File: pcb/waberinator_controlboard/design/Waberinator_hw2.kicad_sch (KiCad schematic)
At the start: 88 parts, among them J1 Conn_01x04_Pin, J17 GX16-4, J18 GX12-4, J19 GX12-4, J2 preconf. cable, J20 GX12-4, J21 GX12-4, J22 GX12-4, J23 GX12-4, J24 GX12-4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

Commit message: [HW] add esp32
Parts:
- removed J4: Conn_01x08_Pin, Connector_PinHeader_2.54mm:PinHeader_1x08_P2.54mm_Vertical, symbol Connector:Conn_01x08_Pin
- added C33, C35: 100nF, Capacitor_SMD:C_0603_1608Metric_Pad1.08x0.95mm_HandSolder, symbol Device:C
- added C34: 100µF, Capacitor_SMD:C_1210_3225Metric_Pad1.33x2.70mm_HandSolder, symbol Device:C
- added C36, C37, C38: 56µF, Capacitor_SMD:C_Elec_5x5.8, symbol Device:C_Polarized
- added FB7: FerriteBead, Capacitor_SMD:C_1210_3225Metric_Pad1.33x2.70mm_HandSolder, symbol Device:FerriteBead
- added J4: Conn_01x06, Connector_PinHeader_2.54mm:PinHeader_1x06_P2.54mm_Vertical, symbol Connector_Generic:Conn_01x06
- added J7: Conn_01x10_Pin, Connector_PinHeader_2.54mm:PinHeader_1x10_P2.54mm_Vertical, symbol Connector:Conn_01x10_Pin
- added Q10, Q8: Q_NPN_BEC, Package_TO_SOT_SMD:SOT-23_Handsoldering, symbol Device:Q_NPN_BEC
- added R1, R2: 100, Resistor_SMD:R_0603_1608Metric_Pad0.98x0.95mm_HandSolder, symbol Device:R
- added R14, R18: 12k, Resistor_SMD:R_0603_1608Metric_Pad0.98x0.95mm_HandSolder, symbol Device:R
- added TP1, TP2, TP3: TestPoint, TestPoint:TestPoint_Pad_1.0x1.0mm, symbol Connector:TestPoint
- added U8: ESP32-WROOM-32, RF_Module:ESP32-WROOM-32, symbol RF_Module:ESP32-WROOM-32
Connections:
- net +3V3: now also C35.1, FB7.1, J7.1 (Pin_1)
- net RET: now also C33.2, C34.2, C35.2, C36.2, C37.2, C38.2, J4.6 (Pin_6), J7.3 (Pin_3), U8.1 (GND), U8.15 (GND), U8.38 (GND), U8.39 (GND)
- net VLed: now also C36.1, C37.1, C38.1
- net ledstring3_drv_en: now also U1.3 (PC14); no longer U1.5 (PF0)
- net ledstring4_drv_en: now also U1.4 (PC15); no longer U1.6 (PF1)
- net swd_swo: now also J7.6 (Pin_6)
- net swd_tck: now also J7.2 (Pin_2)
- net swd_tms: now also J7.4 (Pin_4)
- net usart1_rx_mcu: now also U1.59 (PB7), R1.2; no longer U1.17 (PA3)
- net usart1_tx_mcu: now also U1.58 (PB6), R2.2; no longer U1.16 (PA2)
- net ~{rst}: now also J7.5 (Pin_5)
- net esp32_en: now reaches U1.28 (PB2)
- net esp32_en: now also Q10.3 (C), U8.3 (EN)
- net spare_3: now reaches U1.30 (PB11)
- net spare_3: now also TP1.1
- net spare_4: now reaches U1.33 (PB12)
- net spare_4: now also TP2.1
- net spare_5: now reaches U1.34 (PB13)
- net spare_5: now also TP3.1
- net spare_1: now reaches U1.47 (PF6)
- net spare_1: now also J7.9 (Pin_9)
- net spare_2: now reaches U1.48 (PF7)
- net spare_2: now also J7.10 (Pin_10)
- new net: Q10.1 (B), R14.2
- new net: Q8.1 (B), R18.2
- new net U0RXD_ESP32: J4.3 (Pin_3), U8.34 (RXD0/IO3)
- new net U0TXD_ESP32: J4.2 (Pin_2), U8.35 (TXD0/IO1)
- new net U1RXD_ESP32: R2.1, U8.30 (IO18)
- new net U1TXD_ESP32: R1.1, U8.28 (IO17)
- new net esp32_io0: Q8.3 (C), U8.25 (IO0)
- new net esp32_prog_dtr: J4.1 (Pin_1), Q8.2 (E), R14.1
- new net esp32_prog_rts: J4.5 (Pin_5), Q10.2 (E), R18.1
- new net esp32_vdd: C33.1, C34.1, FB7.2, U8.2 (VDD)
- new net usart2_rx_mcu: J7.7 (Pin_7), U1.17 (PA3)
- new net usart2_tx_mcu: J7.8 (Pin_8), U1.16 (PA2)
- new net vdd_prog: J4.4 (Pin_4)
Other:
- moved on the sheet: J17, J18, J19, J20, J21, J22, J23, J24, J25, J26

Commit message: [HW] finish layout
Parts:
- removed TP3: TestPoint, TestPoint:TestPoint_Pad_1.0x1.0mm, symbol Connector:TestPoint
- added R24: 100, Resistor_SMD:R_0603_1608Metric_Pad0.98x0.95mm_HandSolder, symbol Device:R
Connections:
- net esp32_io0: now also R24.2
- net spare_5: no longer names the net of U1.34 (PB13)
- net spare_5: now also R24.1
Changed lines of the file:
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@@
 	(wire
 		(pts
-			(xy 95.25 236.22) (xy 107.95 236.22)
+			(xy 95.25 236.22) (xy 119.38 236.22)
 		)
 		(stroke
@@
 	(wire
 		(pts
+			(xy 127 236.22) (xy 137.16 236.22)
+		)
+		(stroke
+			(width 0)
+			(type default)
+		)
+	)
+	(wire
+		(pts
 			(xy 335.915 97.155) (xy 356.87 97.155)
 		)
@@
 		)
 	)
+	(label "esp32_io0"
+		(at 127 236.22 0)
+		(fields_autoplaced yes)
+		(effects
+			(font
+				(size 1.27 1.27)
+			)
+			(justify left bottom)
+		)
+	)
 	(label "tim1_ch2_indicator_led2"
 		(at 153.035 247.015 0)
@@
 		)
 	)
-	(label "spare_5"
-		(at 97.79 236.22 0)
-		(fields_autoplaced yes)
-		(effects
-			(font
-				(size 1.27 1.27)
-			)
-			(justify left bottom)
-		)
-	)
 	(label "adc_depth"
 		(at 97.79 162.56 0)
@@
 	)
 	(symbol
-		(lib_id "Connector:TestPoint")
-		(at 107.95 236.22 270)
-		(unit 1)
-		(exclude_from_sim no)
-		(in_bom yes)
-		(on_board yes)
-		(dnp no)
-		(fields_autoplaced yes)
-		(property "Reference" "TP3"
-			(at 113.03 236.22 90)
-			(effects
-				(font
-					(size 1.27 1.27)
-				)
-				(justify left)
-			)
-		)
-		(property "Value" "TestPoint"
-			(at 113.03 237.49 90)
-			(effects
-				(font
-					(size 1.27 1.27)
-				)
-				(justify left)
-				(hide yes)
-			)
-		)
-		(property "Footprint" "TestPoint:TestPoint_Pad_1.0x1.0mm"
-			(at 107.95 241.3 0)
-			(effects
-				(font
-					(size 1.27 1.27)
-				)
-				(hide yes)
-			)
-		)
-		(property "Datasheet" "~"
-			(at 107.95 241.3 0)
-			(effects
-				(font
-					(size 1.27 1.27)
-				)
-				(hide yes)
-			)
-		)
-		(property "Description" ""
-			(at 107.95 236.22 0)
-			(effects
-				(font
-					(size 1.27 1.27)
-				)
-				(hide yes)
-			)
-		)
-		(pin "1"
-		)
-		(instances
-			(project "Waberinator_hw2"
-				(path "/2abe1fd5-5254-4661-ace0-8064915e9450"
-					(reference "TP3")
-					(unit 1)
-				)
-			)
-		)
-	)
-	(symbol
 		(lib_id "Device:C_Polarized")
 		(at 173.355 29.21 0)
@@
 					(unit 1)
 				)
+			)
+		)
+	)
+	(symbol
+		(lib_id "Device:R")
+		(at 123.19 236.22 90)
+		(unit 1)
+		(exclude_from_sim no)
+		(in_bom yes)
+		(on_board yes)
+		(dnp no)
+		(property "Reference" "R24"
+			(at 123.19 236.22 90)
+			(effects
+				(font
+					(size 1.27 1.27)
+				)
+			)
+		)
+		(property "Value" "100"
+			(at 123.19 233.68 90)
+			(effects
+				(font
+					(size 1.27 1.27)
+				)
+			)
+		)
+		(property "Footprint" "Resistor_SMD:R_0603_1608Metric_Pad0.98x0.95mm_HandSolder"
+			(at 123.19 237.998 90)
+			(effects
+				(font
+					(size 1.27 1.27)
+				)
+				(hide yes)
+			)
+		)
+		(property "Datasheet" "~"
+			(at 123.19 236.22 0)
+			(effects
+				(font
+					(size 1.27 1.27)
+				)
+				(hide yes)
+			)
+		)
+		(property "Description" ""
+			(at 123.19 236.22 0)
+			(effects
+				(font
+					(size 1.27 1.27)
+				)
+				(hide yes)
+			)
+		)
+		(pin "2"
+		)
+		(pin "1"
+		)
+		(instances
+			(project "Waberinator_hw2"
+				(path "/2abe1fd5-5254-4661-ace0-8064915e9450"
+					(reference "R24")
+					(unit 1)
+				)

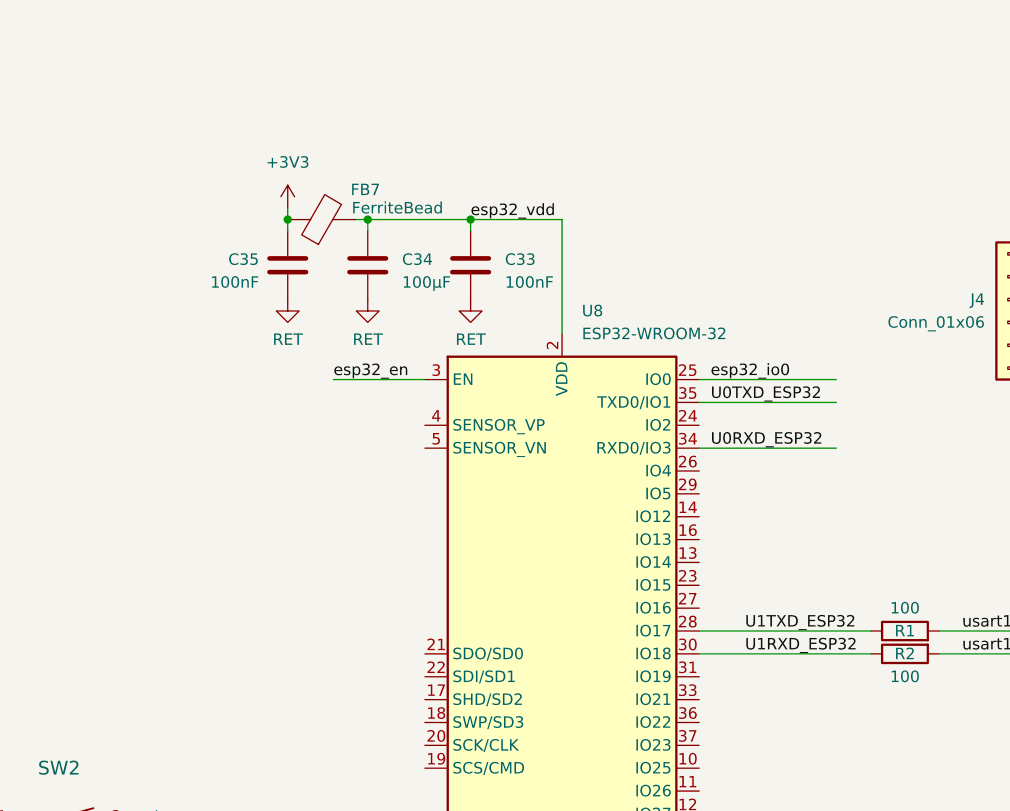
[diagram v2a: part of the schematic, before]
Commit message: [HW/FW] control power state of modem
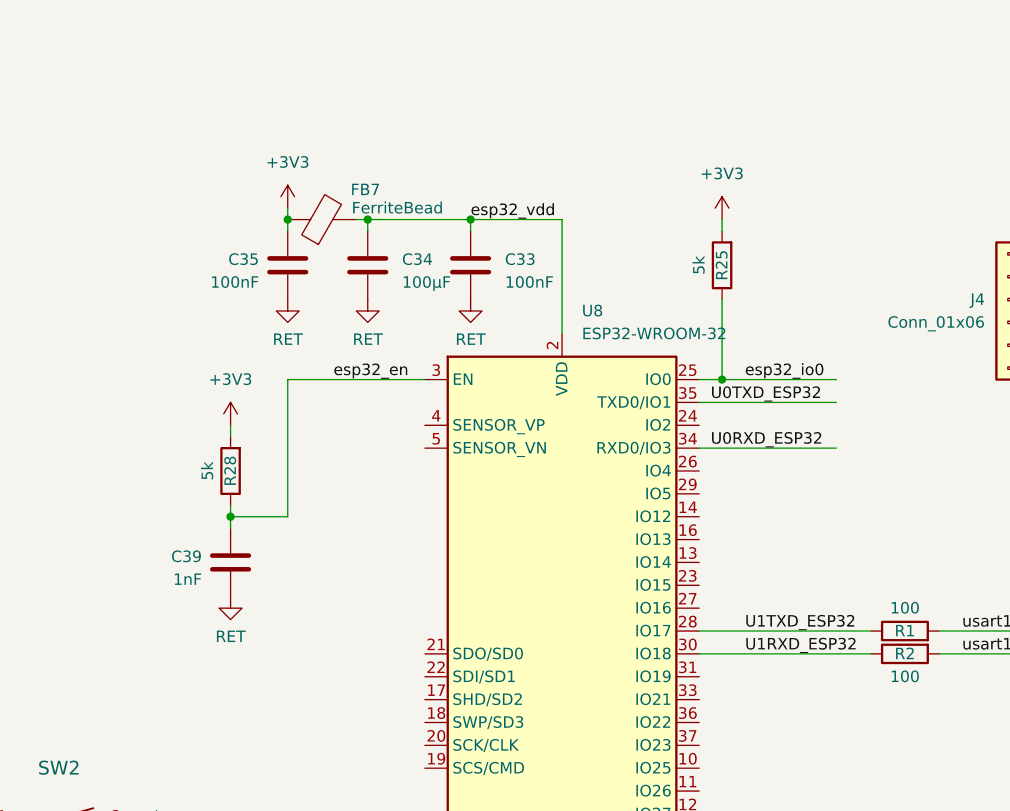
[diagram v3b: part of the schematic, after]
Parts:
- added C39: 1nF, Capacitor_SMD:C_0603_1608Metric_Pad1.08x0.95mm_HandSolder, symbol Device:C
- added R25, R28: 5k, Resistor_SMD:R_0603_1608Metric_Pad0.98x0.95mm_HandSolder, symbol Device:R
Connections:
- net +3V3: now also R25.2, R28.2
- net RET: now also C39.2
- net esp32_en: now also C39.1, R28.1
- net esp32_io0: now also R25.1

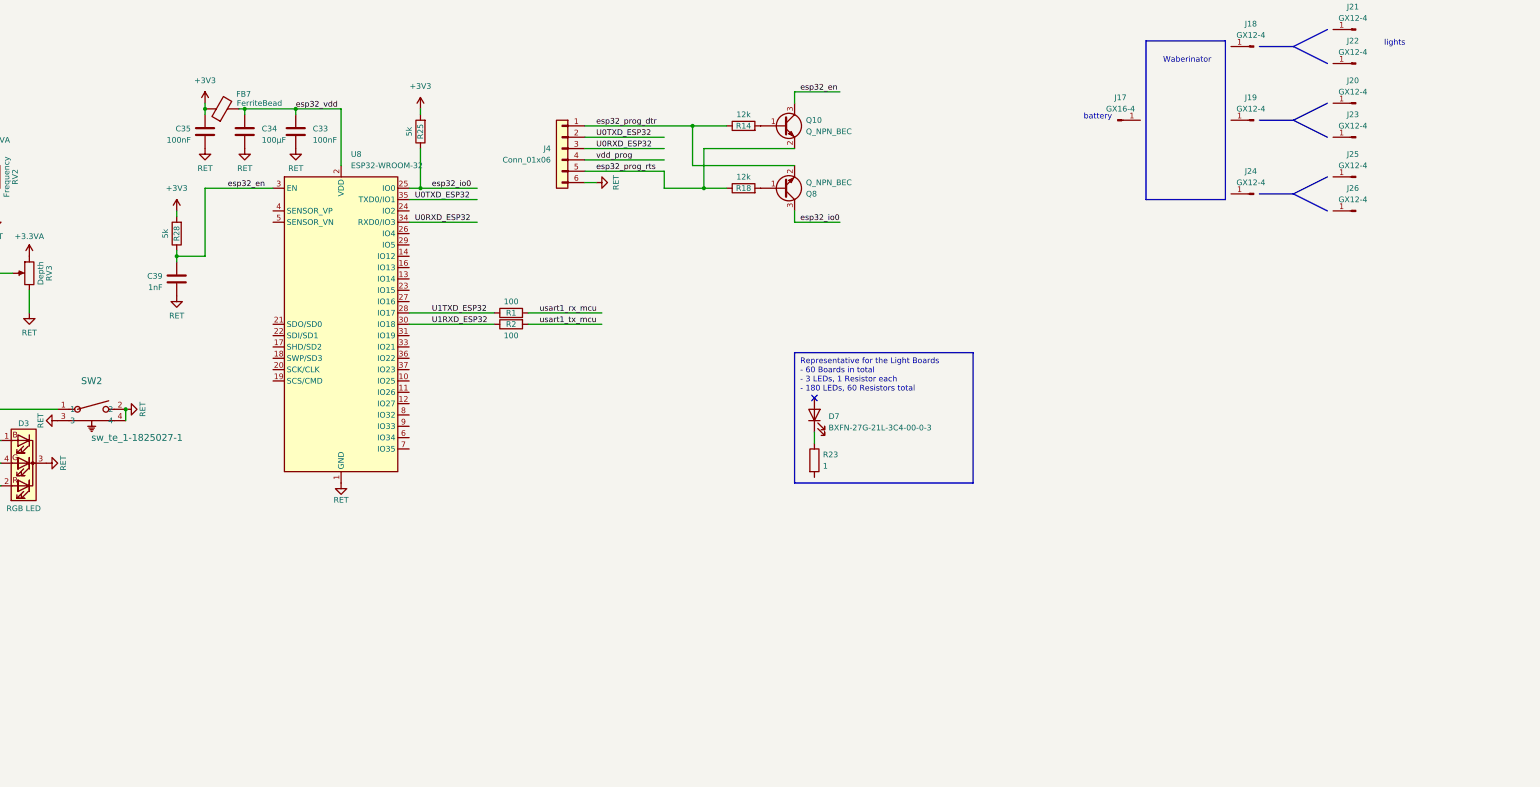
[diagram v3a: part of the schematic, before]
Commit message: [HW] fix esp32 footprint and symbol
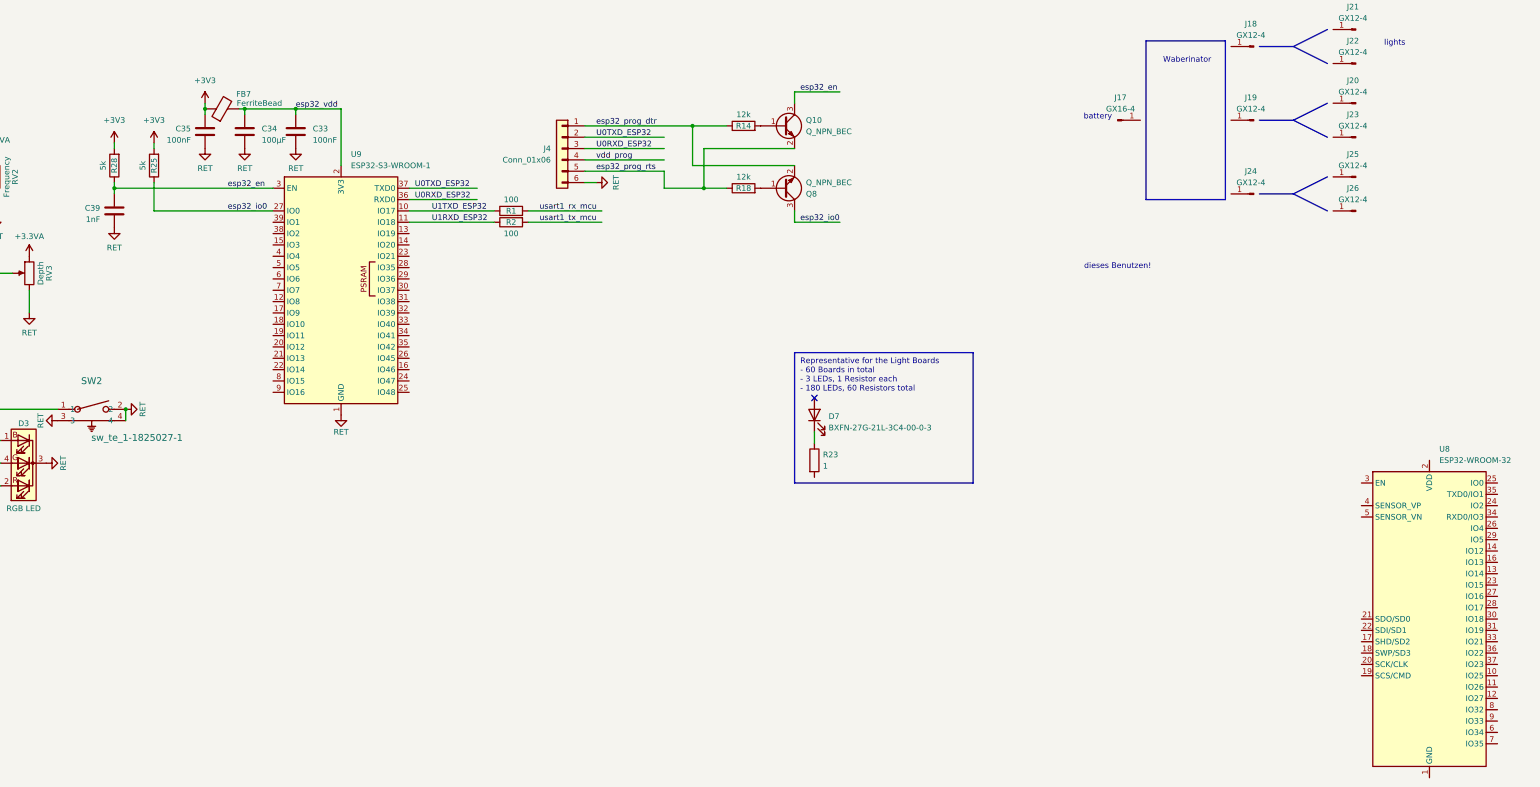
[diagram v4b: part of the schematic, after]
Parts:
- added U9: ESP32-S3-WROOM-1, RF_Module:ESP32-S3-WROOM-1, symbol RF_Module:ESP32-S3-WROOM-1
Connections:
- net RET: now also U9.1 (GND), U9.40 (GND), U9.41 (GND); no longer U8.1 (GND), U8.15 (GND), U8.38 (GND), U8.39 (GND)
- net U0RXD_ESP32: now also U9.36 (RXD0); no longer U8.34 (RXD0/IO3)
- net U0TXD_ESP32: now also U9.37 (TXD0); no longer U8.35 (TXD0/IO1)
- net U1RXD_ESP32: now also U9.11 (IO18); no longer U8.30 (IO18)
- net U1TXD_ESP32: now also U9.10 (IO17); no longer U8.28 (IO17)
- net esp32_en: now also U9.3 (EN); no longer U8.3 (EN)
- net esp32_io0: now also U9.27 (IO0); no longer U8.25 (IO0)
- net esp32_vdd: now also U9.2 (3V3); no longer U8.2 (VDD)
- new net: U8.1 (GND), U8.15 (GND), U8.38 (GND), U8.39 (GND)
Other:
- note added: "dieses Benutzen!"
- moved on the sheet: C39, R1, R2, R25, R28, U8

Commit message: [HW] misc changes
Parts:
- C39: value 1nF -> 1µF
- R14, R18: value 12k -> 10k
- R15, R16: value R -> 120
- R17: value R -> 100
- R25: now not fitted
- R28: value 5k -> 10k
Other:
- note added: "GPIO18 braucht vllt. 10k PU"
- note added: "Itotal = 15.5mA"
- note added: "cts is not the same as rts"
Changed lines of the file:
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@@
 		)
 	)
+	(text "cts is not the same as rts"
+		(exclude_from_sim no)
+		(at 346.964 199.898 0)
+		(effects
+			(font
+				(size 1.27 1.27)
+			)
+		)
+	)
 	(text "battery"
 		(exclude_from_sim no)
@@
 		)
 	)
+	(text "Itotal = 15.5mA"
+		(exclude_from_sim no)
+		(at 213.614 247.396 0)
+		(effects
+			(font
+				(size 1.27 1.27)
+			)
+		)
+	)
 	(text "16V map to 3,2V"
 		(exclude_from_sim no)
@@
 		)
 	)
+	(text "GPIO18 braucht vllt. 10k PU"
+		(exclude_from_sim no)
+		(at 228.092 152.4 0)
+		(effects
+			(font
+				(size 1.27 1.27)
+			)
+		)
+	)
 	(label "tim15_ch2_ledstring6"
 		(at 97.79 241.3 0)
@@
 			)
 		)
-		(property "Value" "12k"
+		(property "Value" "10k"
 			(at 354.33 168.91 90)
 			(effects
@@
 		(in_bom yes)
 		(on_board yes)
-		(dnp no)
+		(dnp yes)
 		(property "Reference" "R25"
 			(at 222.25 180.34 90)
@@
 			)
 		)
-		(property "Value" "1nF"
+		(property "Value" "1µF"
 			(at 210.185 192.405 0)
 			(effects
@@
 			)
 		)
-		(property "Value" "R"
-			(at 182.88 248.285 90)
+		(property "Value" "100"
+			(at 182.88 254.254 90)
 			(effects
 				(font
 					(size 1.27 1.27)
 				)
-				(hide yes)
 			)
 		)
@@
 			)
 		)
-		(property "Value" "R"
-			(at 182.88 239.395 90)
+		(property "Value" "120"
+			(at 182.88 244.094 90)
 			(effects
 				(font
@@
 			)
 		)
-		(property "Value" "R"
-			(at 182.88 243.205 90)
+		(property "Value" "120"
+			(at 182.88 249.174 90)
 			(effects
 				(font
 					(size 1.27 1.27)
 				)
-				(hide yes)
 			)
 		)
@@
 			)
 		)
-		(property "Value" "5k"
+		(property "Value" "10k"
 			(at 210.82 180.34 90)
 			(effects
@@
 			)
 		)
-		(property "Value" "12k"
+		(property "Value" "10k"
 			(at 354.33 182.88 90)
 			(effects

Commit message: [HW] bugfixes
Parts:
- L1: value SRU1048-4R7Y -> 744325330; Digikey SRU1048-4R7YCT-ND -> (none)
- RT1: value 117k -> 95k3
- RV1, RV2, RV3: Digikey 118-3310C-025-103L-ND -> 3310C-001-103L-ND
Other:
- note added: "eventuell durch 744325330 (3,3µH) oder 7443320470 (4,7µH) ersetzen"
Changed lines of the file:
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@@
 		)
 	)
+	(text "eventuell durch 744325330 (3,3µH) oder 7443320470 (4,7µH) ersetzen"
+		(exclude_from_sim no)
+		(at 295.656 23.622 0)
+		(effects
+			(font
+				(size 1.27 1.27)
+			)
+		)
+	)
 	(text "Waberinator"
 		(exclude_from_sim no)
@@
 			)
 		)
-		(property "Digikey" "118-3310C-025-103L-ND"
+		(property "Digikey" "  3310C-001-103L-ND"
 			(at 186.69 182.88 90)
 			(effects
@@
 			)
 		)
-		(property "Digikey" "118-3310C-025-103L-ND"
+		(property "Digikey" "  3310C-001-103L-ND"
 			(at 194.31 204.47 90)
 			(effects
@@
 			)
 		)
-		(property "Value" "117k"
+		(property "Value" "95k3"
 			(at 199.39 55.88 0)
 			(effects
@@
 			)
 		)
-		(property "Digikey" "118-3310C-025-103L-ND"
+		(property "Digikey" "  3310C-001-103L-ND"
 			(at 179.705 161.29 90)
 			(effects
@@
 			)
 		)
-		(property "Value" "SRU1048-4R7Y"
+		(property "Value" "744325330"
 			(at 266.7 30.48 90)
 			(effects
@@
 			)
 		)
-		(property "Digikey" " SRU1048-4R7YCT-ND"
+		(property "Digikey" ""
 			(at 266.7 34.29 0)
 			(effects
